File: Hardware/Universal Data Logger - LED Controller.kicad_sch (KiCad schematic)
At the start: 0 parts

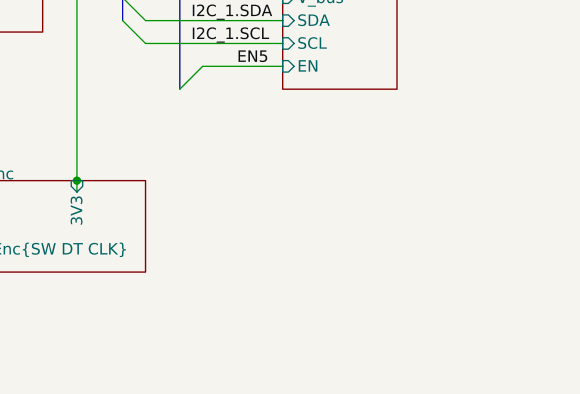
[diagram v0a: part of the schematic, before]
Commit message: Added RTC chip
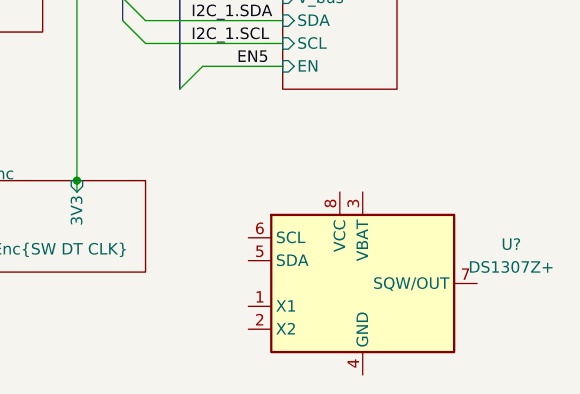
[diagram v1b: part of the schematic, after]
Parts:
- added U?: DS1307Z+, Package_SO:SOIC-8_3.9x4.9mm_P1.27mm, symbol Timer_RTC:DS1307Z+

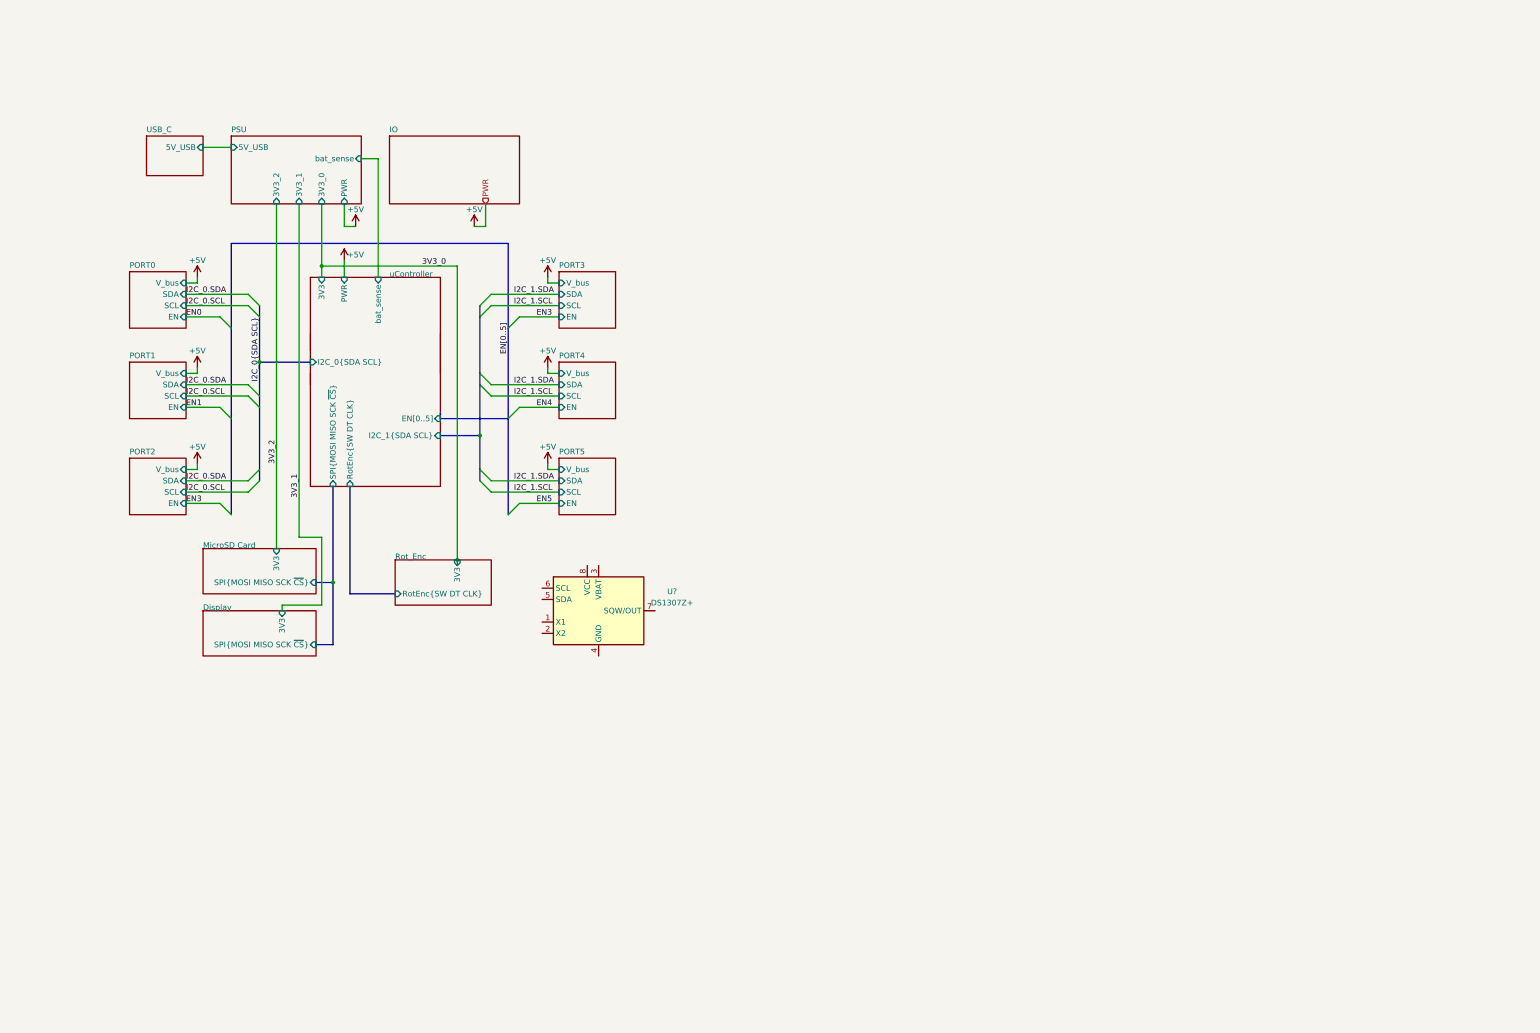
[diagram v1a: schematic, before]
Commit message: changed Schematic and added RTC
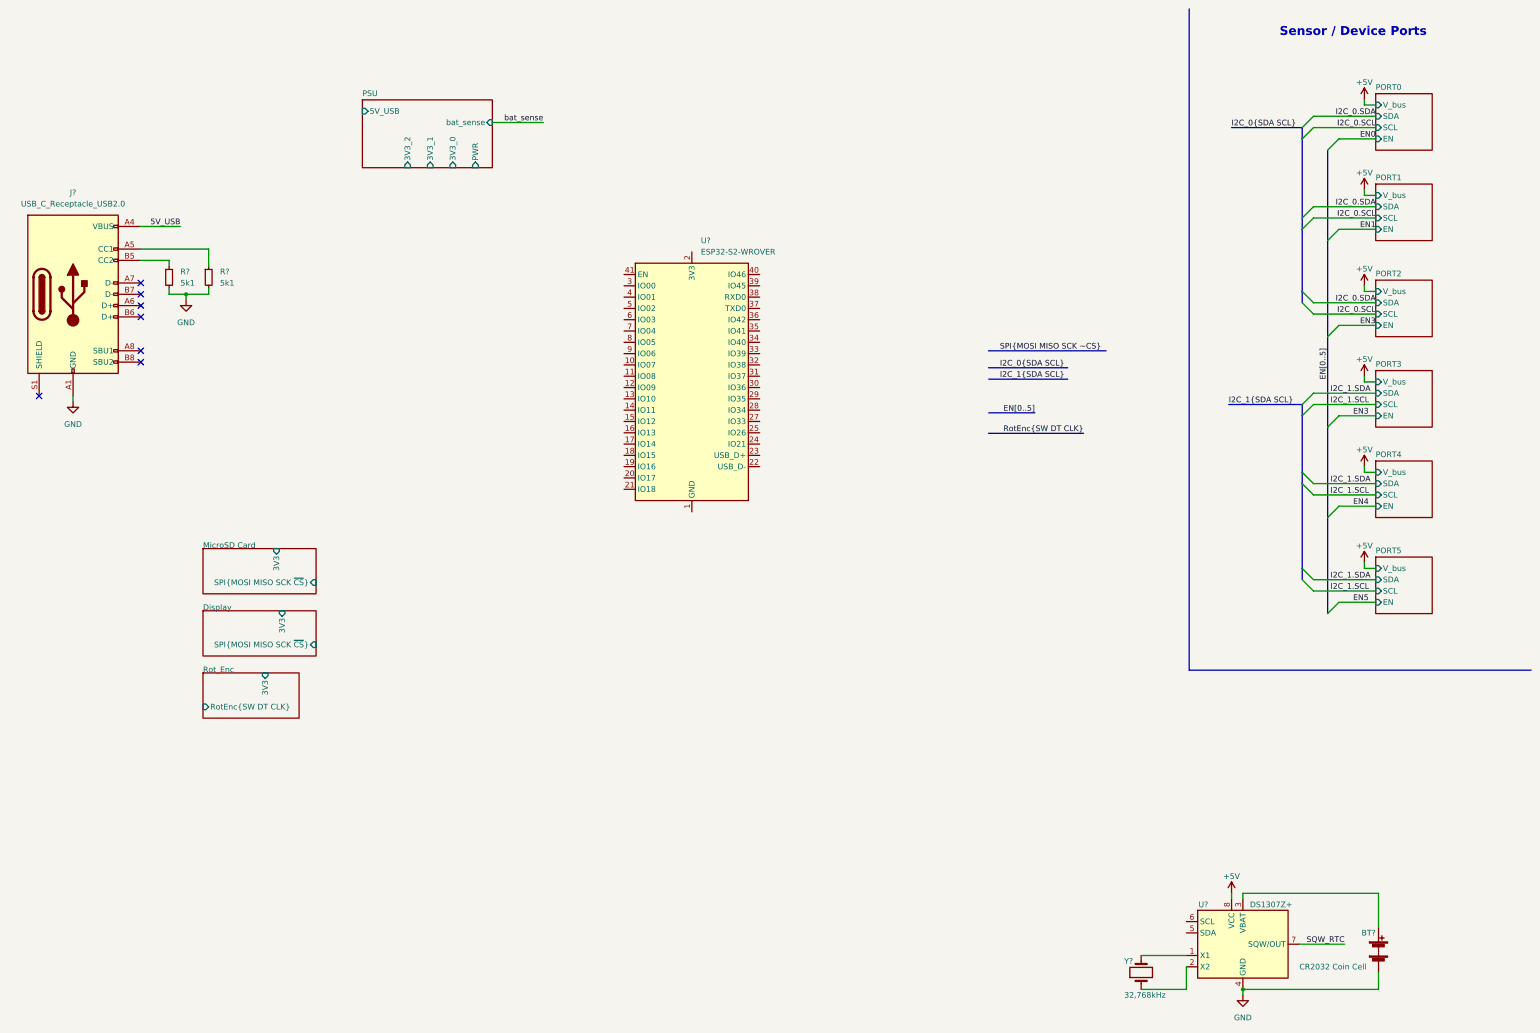
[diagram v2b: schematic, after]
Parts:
- added BT?: CR2032 Coin Cell, symbol Device:Battery
- added J?: USB_C_Receptacle_USB2.0, symbol Connector:USB_C_Receptacle_USB2.0
- added R? (x2): 5k1, symbol Device:R_Small
- added U?: ESP32-S2-WROVER, RF_Module:ESP32-S2-WROVER, symbol RF_Module:ESP32-S2-WROVER
- added Y?: 32,768kHz, symbol Device:Crystal
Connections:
- net +5V: now also U?.8 (VCC)
- net at U?.1 (X1): now also Y?.2
- net at U?.2 (X2): now also Y?.1
- net at U?.3 (VBAT): now also BT?.1 (+)
- net GND: now reaches U?.4 (GND)
- net GND: now also BT?.2 (-), J?.A1 (GND), J?.A12 (GND), J?.B1 (GND), J?.B12 (GND), R?.2, R?.2
- net SQW_RTC: now reaches U?.7 (SQW/OUT)
- new net: U?.1 (GND), U?.26 (GND), U?.42 (GND), U?.43 (GND)
- new net: J?.B5 (CC2), R?.1
- new net: J?.A5 (CC1), R?.1
- new net 5V_USB: J?.A4 (VBUS), J?.A9 (VBUS), J?.B4 (VBUS), J?.B9 (VBUS)
- no-connect marks 0 -> 7
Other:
- removed sheet IO
- removed sheet USB_C
- removed sheet uController
- note added: "Sensor / Device Ports"
- moved on the sheet: U?

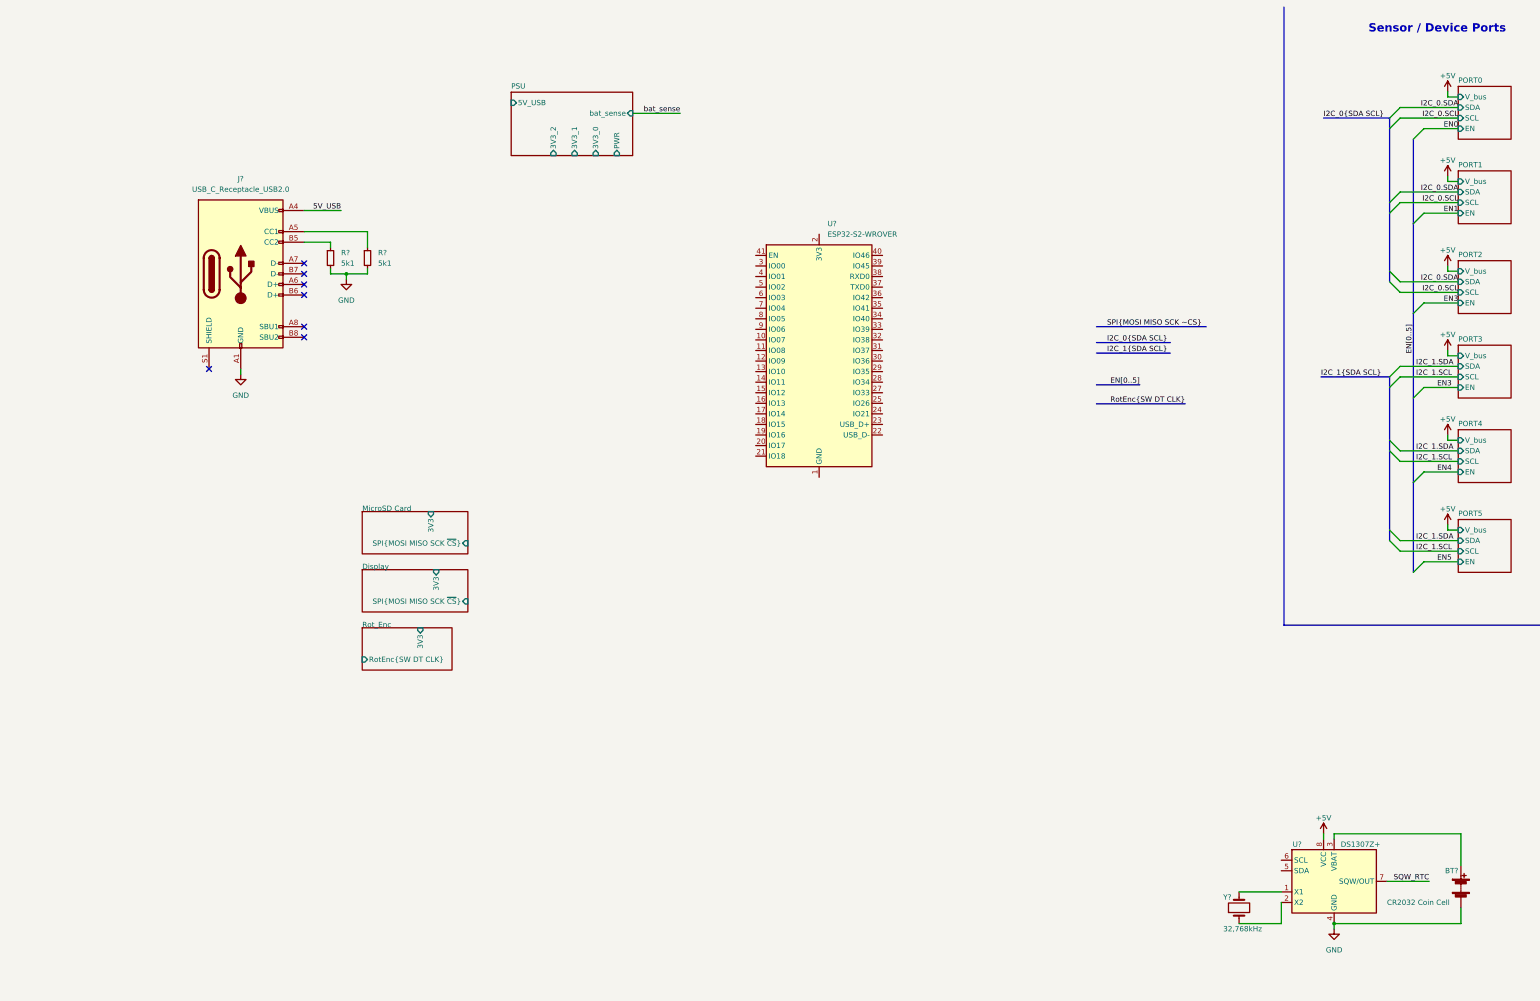
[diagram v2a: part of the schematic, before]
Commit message: added reset line and connected things
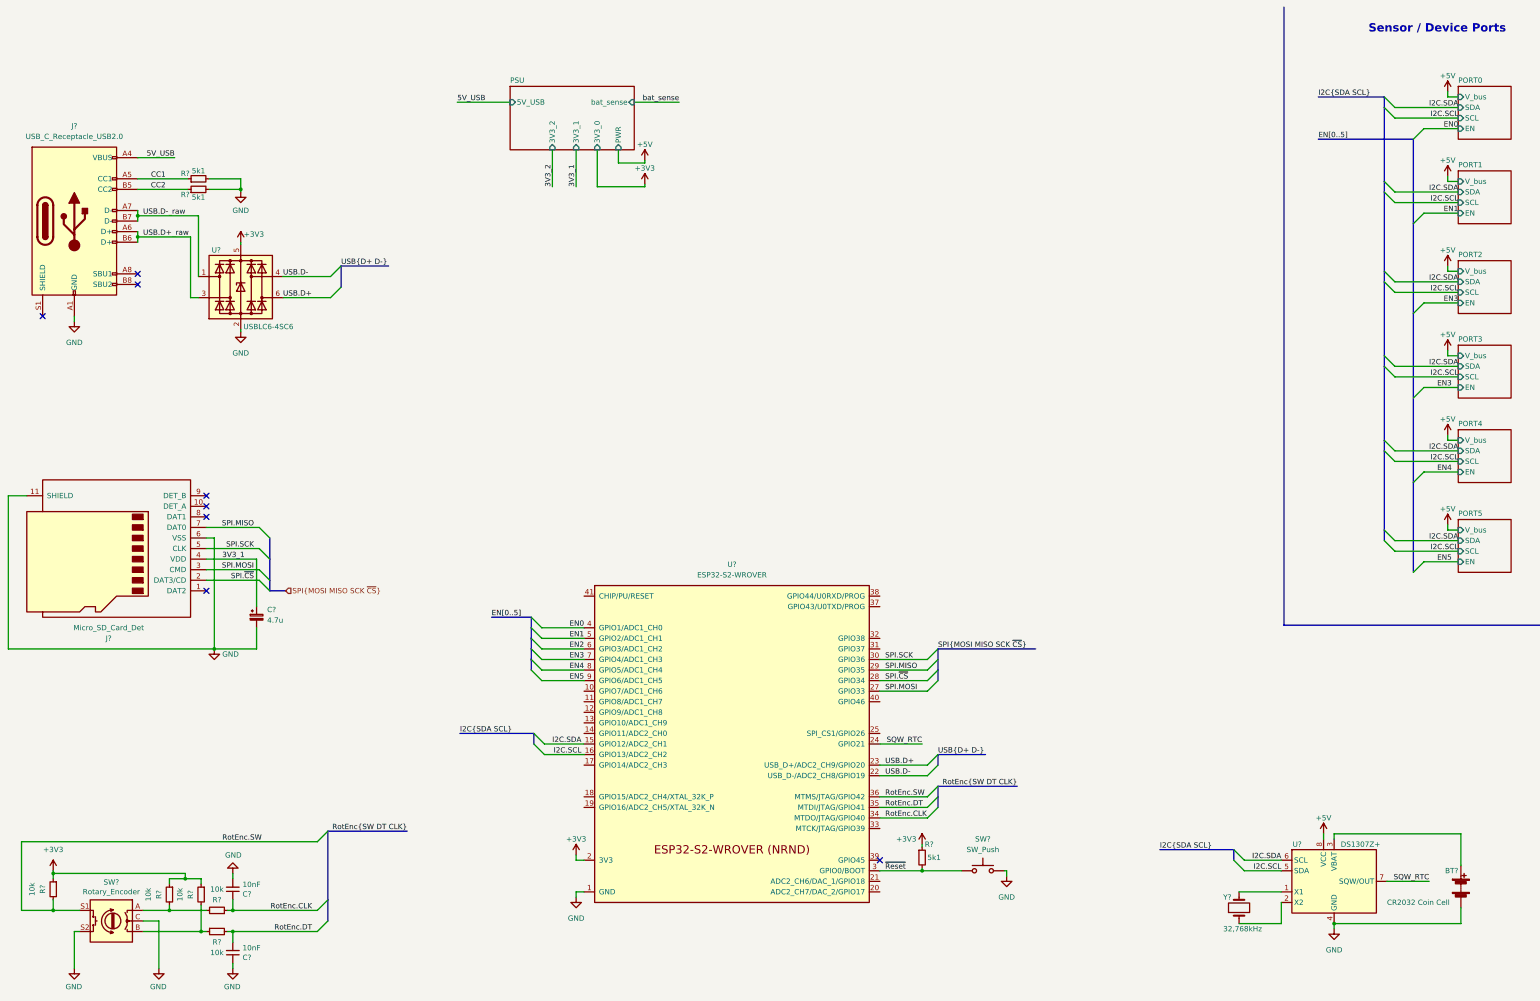
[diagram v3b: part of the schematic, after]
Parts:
- removed U?: ESP32-S2-WROVER, RF_Module:ESP32-S2-WROVER, symbol RF_Module:ESP32-S2-WROVER
- added C?: 4.7u, symbol Device:C_Polarized_Small
- added C? (x2): 10nF, Capacitor_SMD:C_0805_2012Metric_Pad1.15x1.40mm_HandSolder, symbol Device:C_Small
- added J?: Micro_SD_Card_Det, symbol Connector:Micro_SD_Card_Det
- added R? (x5): 10k, Resistor_SMD:R_0805_2012Metric_Pad1.20x1.40mm_HandSolder, symbol Device:R_Small
- added R?: 5k1, symbol Device:R_Small
- added SW?: SW_Push, symbol Switch:SW_Push
- added SW?: Rotary_Encoder, Rotary_Encoder:RotaryEncoder_Alps_EC12E-Switch_Vertical_H20mm, symbol Device:Rotary_Encoder_Switch
- added U?: USBLC6-4SC6, Package_TO_SOT_SMD:SOT-23-6, symbol Power_Protection:USBLC6-4SC6
- added U?: ESP32-S2-WROVER, Espressif:ESP32-S2-WROVER, symbol Espressif:ESP32-S2-WROVER
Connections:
- net EN0: now also U?.4 (GPIO1/ADC1_CH0)
- net EN1: now also U?.5 (GPIO2/ADC1_CH1)
- net EN3: now also U?.7 (GPIO4/ADC1_CH3)
- net EN4: now also U?.8 (GPIO5/ADC1_CH4)
- net EN5: now also U?.9 (GPIO6/ADC1_CH5)
- net GND: now also C?.1, C?.2, C?.2, J?.11 (SHIELD), J?.6 (VSS), SW?.2, SW?.C, SW?.S2, U?.1 (GND), U?.2 (GND), U?.26 (GND), U?.42 (GND), U?.43 (GND)
- net SQW_RTC: now also U?.24 (GPIO21)
- net I2C.SCL: now reaches U?.5 (SDA)
- net I2C.SCL: now also U?.16 (GPIO13/ADC2_CH2)
- net I2C.SDA: now reaches U?.6 (SCL)
- net I2C.SDA: now also U?.15 (GPIO12/ADC2_CH1)
- net CC2: now reaches J?.B5 (CC2), R?.1
- net CC1: now reaches J?.A5 (CC1), R?.1
- net USB.D+_raw: now reaches J?.A6 (D+)
- net USB.D+_raw: now also J?.B6 (D+), U?.3 (I/O2)
- net USB.D-_raw: now reaches J?.A7 (D-)
- net USB.D-_raw: now also J?.B7 (D-), U?.1 (I/O1)
- new net: R?.1, R?.2, SW?.B
- new net: R?.2, R?.2, SW?.A
- new net +3V3: R?.1, R?.1, R?.1, R?.1, U?.2 (3V3), U?.5 (VBUS)
- new net 3V3_1: C?.1, J?.4 (VDD)
- new net EN2: U?.6 (GPIO3/ADC1_CH2)
- new net RotEnc.CLK: C?.1, R?.1, U?.34 (MTDO/JTAG/GPIO40)
- new net RotEnc.DT: C?.2, R?.2, U?.35 (MTDI/JTAG/GPIO41)
- new net RotEnc.SW: R?.2, SW?.S1, U?.36 (MTMS/JTAG/GPIO42)
- new net SPI.MISO: J?.7 (DAT0), U?.29 (GPIO35)
- new net SPI.MOSI: J?.3 (CMD), U?.27 (GPIO33)
- new net SPI.SCK: J?.5 (CLK), U?.30 (GPIO36)
- new net SPI.~{CS}: J?.2 (DAT3/CD), U?.28 (GPIO34)
- new net USB.D+: U?.23 (USB_D+/ADC2_CH9/GPIO20), U?.6 (I/O4)
- new net USB.D-: U?.22 (USB_D-/ADC2_CH8/GPIO19), U?.4 (I/O3)
- new net ~{Reset}: R?.2, SW?.1, U?.3 (GPIO0/BOOT)
- no-connect marks 7 -> 8
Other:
- removed sheet Display
- removed sheet MicroSD Card
- removed sheet Rot_Enc
- moved on the sheet: J?, R?
